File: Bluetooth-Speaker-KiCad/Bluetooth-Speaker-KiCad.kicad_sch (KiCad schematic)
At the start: 34 parts, among them J1 USB4105-GF-A, J2 Screw_Terminal_01x02, J3 Screw_Terminal_01x02, Q1 Q_PMOS_DSG, SW1 SW_Push, SW2 SW_Push, U1 TPD4E02B04DQA, U2 MAX1811, U3 RT6150B-33GQW, U5 ESP32-C3-WROOM-02, U6 MAX98357A

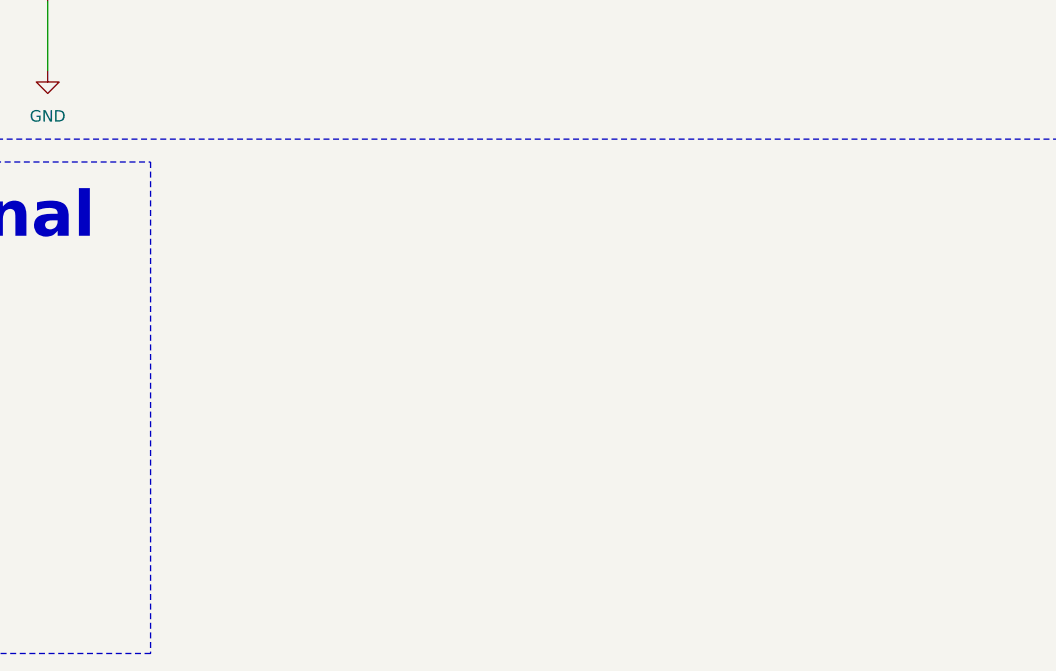
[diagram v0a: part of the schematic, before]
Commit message: Removed mounting holes
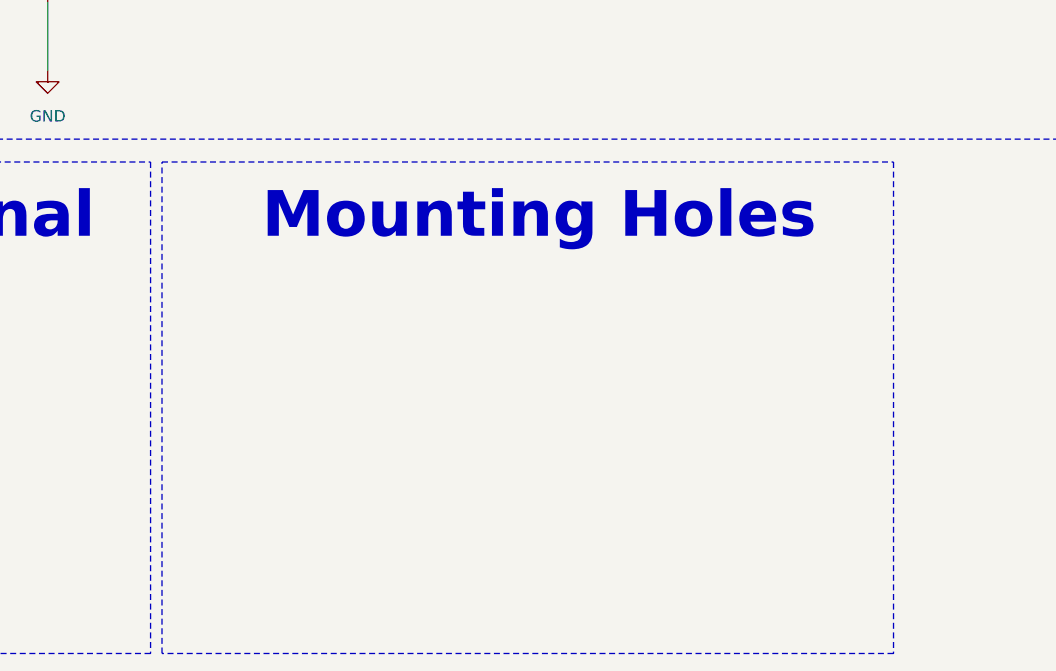
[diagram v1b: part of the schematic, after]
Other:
- note added: "Mounting Holes"
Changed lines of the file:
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@@
+	)
+	(rectangle
+		(start 102.87 219.71)
+		(end 184.15 274.32)
+		(stroke
+			(width 0)
+			(type dash)
+		)
+		(fill
+			(type none)
+		)
 	)
 	(rectangle
@@
 		(effects
 			(font
+				(size 5.08 5.08)
+				(thickness 1.016)
+				(bold yes)
+			)
+		)
+	)
+	(text "Mounting Holes"
+		(exclude_from_sim no)
+		(at 144.78 225.806 0)
+		(effects
+			(font

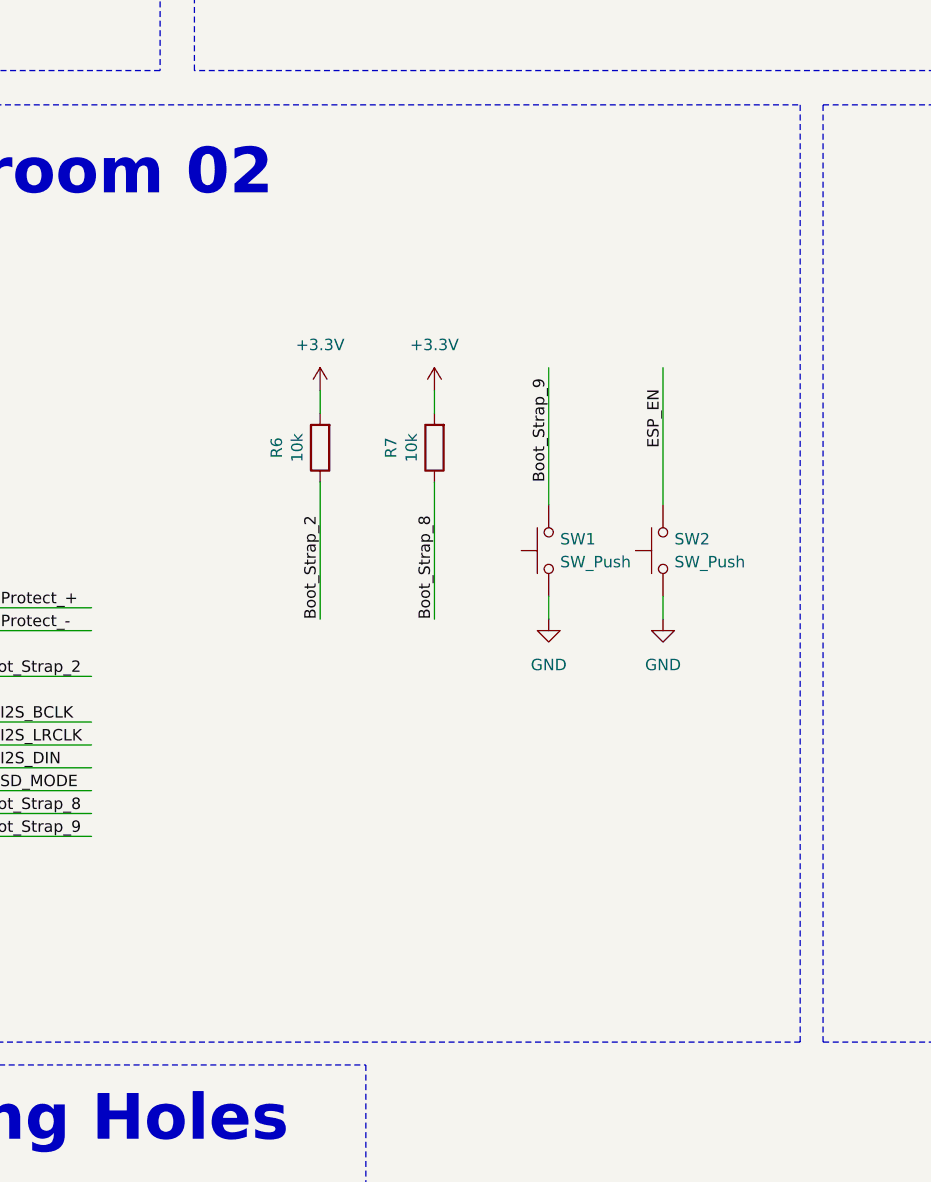
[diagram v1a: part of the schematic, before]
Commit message: Updated layout with switches
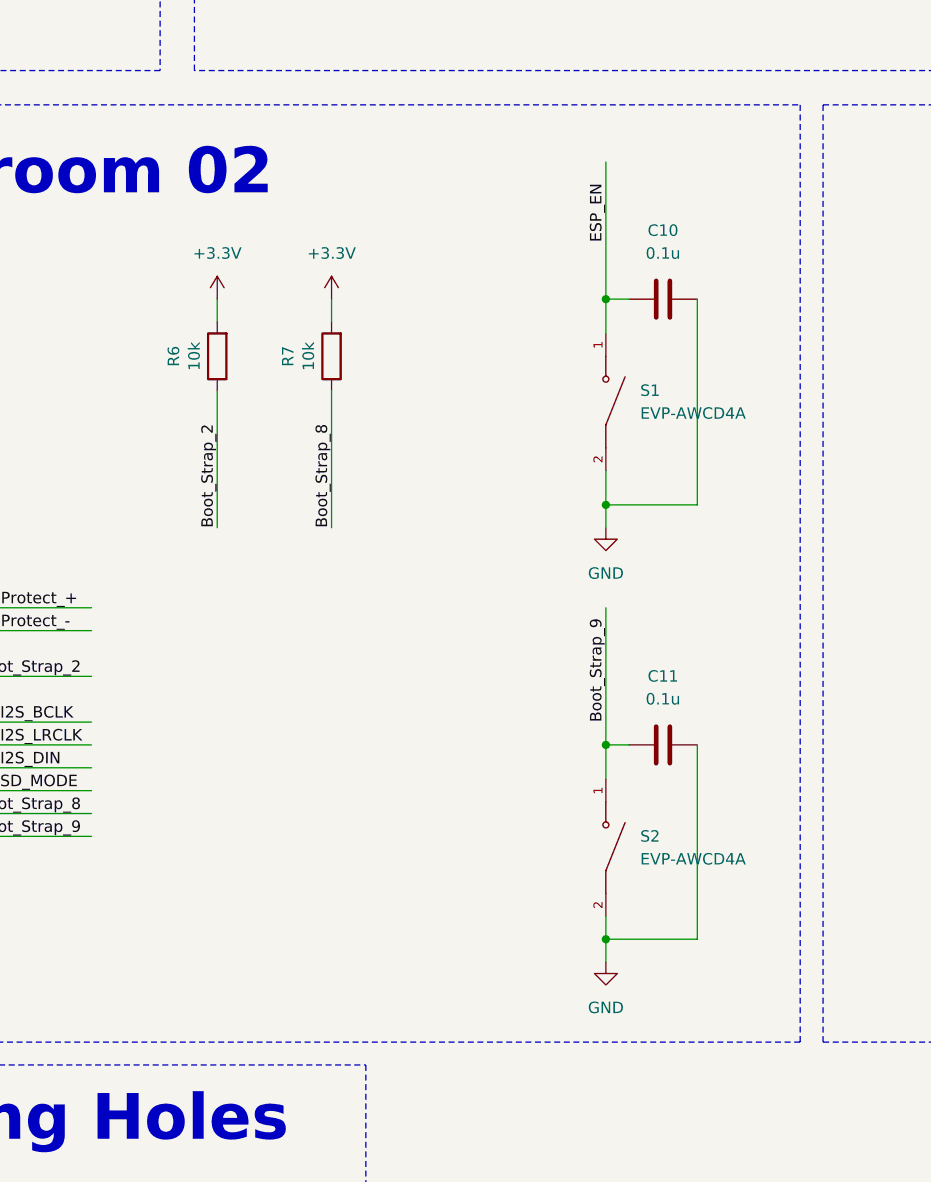
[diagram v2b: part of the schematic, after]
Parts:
- removed SW1, SW2: SW_Push, symbol Switch:SW_Push
- added C10, C11: 0.1u, Capacitor_SMD:C_0603_1608Metric_Pad1.08x0.95mm_HandSolder, symbol Device:C
- added S1, S2: EVP-AWCD4A, EVP_AWCD4A (1):SW_EVP-AWCD4A, symbol EVP-AWCD4A:EVP-AWCD4A
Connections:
- net Boot_Strap_9: now also C11.1, S2.1
- net ESP_EN: now also C10.1, S1.1
- net GND: now also C10.2, C11.2, S1.2, S2.2
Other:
- moved on the sheet: R6, R7
